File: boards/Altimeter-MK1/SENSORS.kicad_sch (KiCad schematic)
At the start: 21 parts, among them U301 SAM-M8Q-0-10, U302 MS5611-01BA, U303 LSM9DS1, U304 H3LIS331DL

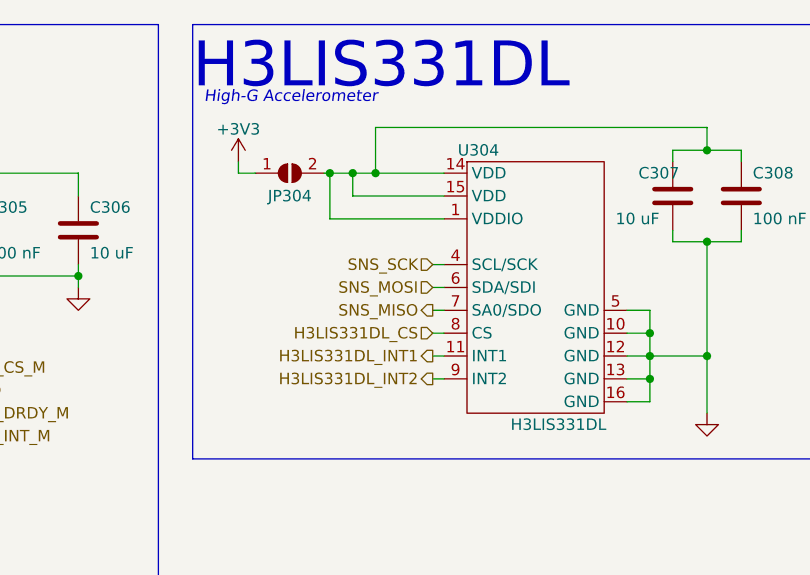
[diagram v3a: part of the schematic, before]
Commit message: Organized schematics and labels
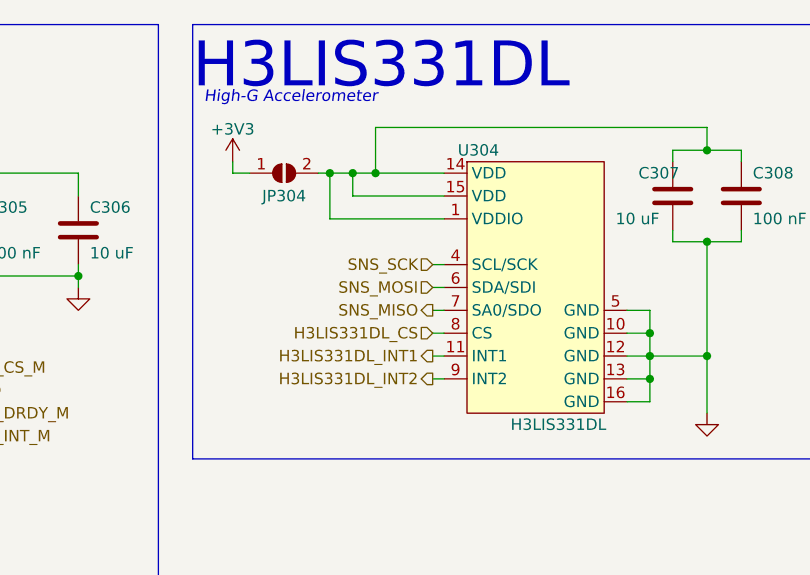
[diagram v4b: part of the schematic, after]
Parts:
- C301, C302, C303, C304, C305, C306, C307, C308: footprint (none) -> Capacitor_SMD:C_0402_1005Metric
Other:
- moved on the sheet: JP304
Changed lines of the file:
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@@
     (stroke (width 0) (type default) (color 0 0 0 0))
   )
-  (wire (pts (xy 181.61 30.48) (xy 181.61 31.75))
+  (wire (pts (xy 180.975 30.48) (xy 180.975 31.75))
     (stroke (width 0) (type default) (color 0 0 0 0))
   )
@@
     (stroke (width 0) (type default) (color 0 0 0 0))
   )
-  (wire (pts (xy 181.61 31.75) (xy 183.515 31.75))
+  (wire (pts (xy 180.975 31.75) (xy 182.88 31.75))
     (stroke (width 0) (type default) (color 0 0 0 0))
   )
@@
     (stroke (width 0) (type default) (color 0 0 0 0))
   )
-  (wire (pts (xy 191.135 31.75) (xy 191.77 31.75))
+  (wire (pts (xy 190.5 31.75) (xy 191.77 31.75))
     (stroke (width 0) (type default) (color 0 0 0 0))
   )
@@
       (effects (font (size 1.27 1.27)) (justify left))
     )
-    (property "Footprint" "" (id 2) (at 238.4552 38.1 0)
+    (property "Footprint" "Capacitor_SMD:C_0402_1005Metric" (id 2) (at 238.4552 38.1 0)
       (effects (font (size 1.27 1.27)) hide)
     )
@@
     (pin "1")
   )
-  (symbol (lib_id "power:+3V3") (at 181.61 30.48 0) (unit 1)
-    (in_bom yes) (on_board yes) (fields_autoplaced)
-    (property "Reference" "#PWR0308" (id 0) (at 181.61 34.29 0)
-      (effects (font (size 1.27 1.27)) hide)
-    )
-    (property "Value" "+3V3" (id 1) (at 181.61 26.8755 0))
-    (property "Footprint" "" (id 2) (at 181.61 30.48 0)
-      (effects (font (size 1.27 1.27)) hide)
-    )
-    (property "Datasheet" "" (id 3) (at 181.61 30.48 0)
-      (effects (font (size 1.27 1.27)) hide)
-    )
-    (pin "1")
-  )
-  (symbol (lib_id "Jumper:SolderJumper_2_Open") (at 187.325 31.75 0) (unit 1)
-    (in_bom yes) (on_board yes)
-    (property "Reference" "JP304" (id 0) (at 187.325 34.29 0))
-    (property "Value" "SolderJumper_2_Open" (id 1) (at 186.055 35.56 0)
-      (effects (font (size 1.27 1.27)) hide)
-    )
-    (property "Footprint" "Jumper:SolderJumper-2_P1.3mm_Open_RoundedPad1.0x1.5mm" (id 2) (at 187.325 31.75 0)
-      (effects (font (size 1.27 1.27)) hide)
-    )
-    (property "Datasheet" "~" (id 3) (at 187.325 31.75 0)
+  (symbol (lib_id "power:+3V3") (at 180.975 30.48 0) (unit 1)
+    (in_bom yes) (on_board yes) (fields_autoplaced)
+    (property "Reference" "#PWR0308" (id 0) (at 180.975 34.29 0)
+      (effects (font (size 1.27 1.27)) hide)
+    )
+    (property "Value" "+3V3" (id 1) (at 180.975 26.8755 0))
+    (property "Footprint" "" (id 2) (at 180.975 30.48 0)
+      (effects (font (size 1.27 1.27)) hide)
+    )
+    (property "Datasheet" "" (id 3) (at 180.975 30.48 0)
+      (effects (font (size 1.27 1.27)) hide)
+    )
+    (pin "1")
+  )
+  (symbol (lib_id "Jumper:SolderJumper_2_Open") (at 186.69 31.75 0) (unit 1)
+    (in_bom yes) (on_board yes)
+    (property "Reference" "JP304" (id 0) (at 186.69 34.29 0))
+    (property "Value" "SolderJumper_2_Open" (id 1) (at 185.42 35.56 0)
+      (effects (font (size 1.27 1.27)) hide)
+    )
+    (property "Footprint" "Jumper:SolderJumper-2_P1.3mm_Open_RoundedPad1.0x1.5mm" (id 2) (at 186.69 31.75 0)
+      (effects (font (size 1.27 1.27)) hide)
+    )
+    (property "Datasheet" "~" (id 3) (at 186.69 31.75 0)
       (effects (font (size 1.27 1.27)) hide)
     )
@@
       (effects (font (size 1.27 1.27)) (justify left))
     )
-    (property "Footprint" "" (id 2) (at 164.7952 41.91 0)
+    (property "Footprint" "Capacitor_SMD:C_0402_1005Metric" (id 2) (at 164.7952 41.91 0)
       (effects (font (size 1.27 1.27)) hide)
     )
@@
       (effects (font (size 1.27 1.27)) (justify left))
     )
-    (property "Footprint" "" (id 2) (at 153.3652 41.91 0)
+    (property "Footprint" "Capacitor_SMD:C_0402_1005Metric" (id 2) (at 153.3652 41.91 0)
       (effects (font (size 1.27 1.27)) hide)
     )
@@
       (effects (font (size 1.27 1.27)) (justify left))
     )
-    (property "Footprint" "" (id 2) (at 141.9352 41.91 0)
+    (property "Footprint" "Capacitor_SMD:C_0402_1005Metric" (id 2) (at 141.9352 41.91 0)
       (effects (font (size 1.27 1.27)) hide)
     )
@@
       (effects (font (size 1.27 1.27)) (justify left))
     )
-    (property "Footprint" "" (id 2) (at 230.8352 38.1 0)
+    (property "Footprint" "Capacitor_SMD:C_0402_1005Metric" (id 2) (at 230.8352 38.1 0)
       (effects (font (size 1.27 1.27)) hide)
     )
@@
       (effects (font (size 1.27 1.27)) (justify left))
     )
-    (property "Footprint" "" (id 2) (at 107.6452 88.9 0)
+    (property "Footprint" "Capacitor_SMD:C_0402_1005Metric" (id 2) (at 107.6452 88.9 0)
       (effects (font (size 1.27 1.27)) hide)
     )
@@
       (effects (font (size 1.27 1.27)) (justify left))
     )
-    (property "Footprint" "" (id 2) (at 96.2152 88.9 0)
+    (property "Footprint" "Capacitor_SMD:C_0402_1005Metric" (id 2) (at 96.2152 88.9 0)
       (effects (font (size 1.27 1.27)) hide)
     )
@@
       (effects (font (size 1.27 1.27)) (justify left))
     )
-    (property "Footprint" "" (id 2) (at 69.5452 100.33 0)
-      (effects (font (size 1.27 1.27)) hide)
-    )
+    (property "Footprint" "Capacitor_SMD:C_0402_1005Metric" (id 2) (at 69.5452 100.33 0)
+      (effects (font (size 1.27 1.27)) hide)
+    )

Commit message: Assigned more footprints and pin connections
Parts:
- U301: footprint (none) -> RF_GPS:ublox_SAM-M8Q
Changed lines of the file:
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@@
       (effects (font (size 1.27 1.27)) (justify left))
     )
-    (property "Footprint" "" (id 2) (at 62.23 55.88 0)
+    (property "Footprint" "RF_GPS:ublox_SAM-M8Q" (id 2) (at 62.23 55.88 0)
       (effects (font (size 1.27 1.27)) hide)
     )
